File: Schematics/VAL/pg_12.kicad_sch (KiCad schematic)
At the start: 19 parts, among them U1401 F04, U1402 F04, U1403 F04, U1404 F04, U1405 F04, U1406 F04, U1407 F04, U1408 F04, U1409 F04, U1410 F04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

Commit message: Align to grid
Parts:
- removed U1401, U1402, U1403, U1404, U1405, U1406, U1407, U1408, U1409, U1410, U1411, U1412: F04, symbol r1000:F04
- removed U1413, U1414: F64, symbol r1000:F64
- removed U1415, U1416, U1417: F00, symbol r1000:F00
- removed U1418: F240, symbol r1000:F240
- removed U1419: F374, symbol r1000:F374
- added U (x12): (no value), symbol r1000:F04
- added U (x3): (no value), symbol r1000:F00
- added U: (no value), symbol r1000:F374
- added U (x2): (no value), symbol r1000:F64
- added U: (no value), symbol r1000:F240
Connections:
- net A.D48: now also U.18 (Y0)
- net A.D49: now also U.16 (Y1)
- net A.D50: now also U.14 (Y2)
- net A.D51: now also U.12 (Y3)
- net A.D52: now also U.9 (Y4)
- net A.D53: now also U.7 (Y5)
- net A.D54: now also U.5 (Y6)
- net A.D55: now also U.3 (Y7)
- net A.D56: now also U.2 (Q0)
- net A.D57: now also U.5 (Q1)
- net A.D58: now also U.6 (Q2)
- net A.D59: now also U.9 (Q3)
- net A.D60: now also U.12 (Q4)
- net A.D61: now also U.15 (Q5)
- net A.D62: now also U.16 (Q6)
- net A.D63: now also U.19 (Q7)
- net ALU.ZERO0: now also U.1 (D0)
- net ALU.ZERO1: now also U.1 (D0)
- net ALU.ZERO2: now also U.1 (D0)
- net ALU.ZERO3: now also U.1 (D0)
- net ALU.ZERO4: now also U.1 (D0)
- net ALU.ZERO5: now also U.1 (D0)
- net ALU.ZERO6: now also U.1 (D0)
- net ALU_32_Z~: now also U.1 (D0)
- net ALU_EQ_Z~: now also U.1 (D0), U.1 (D0), U.1 (D0), U.4 (D1)
- net PD: now also U.11 (I4), U.13 (I5), U.15 (I6), U.17 (I7), U.2 (I0), U.4 (I1), U.6 (I2), U.8 (I3)
- net PU: now also U.13 (D3), U.2 (A0), U.2 (A0), U.3 (D0), U.9 (B0)
- net ZERO.OE~: now also U.1 (OE), U.1 (OE0), U.19 (OE1)
- net ZERO_COUNT~1: now also U.3 (Q), U.7 (D2)
- net ZERO_COUNT~2: now also U.3 (Q), U.8 (D3)
- net ZERO_COUNT~3: now also U.13 (D4), U.3 (Q)
- net ZERO_COUNT~4: now also U.14 (D5)
- net ZERO_COUNT~5: now also U.17 (D6)
- net ZERO_COUNT~6: now also U.18 (D7)
- net ZERO~.SCLK: now also U.11 (CLK)
- net ZMUX.SEL0: now also U.2 (D1), U.2 (Q)
- net ZMUX.SEL1: now also U.2 (D1), U.8 (Q)
- net ZMUX.SEL2: now also U.2 (D1), U.8 (Q)
- new net: U.1 (D0), U.2 (Q), U.3 (A1)
- new net: U.10 (B1), U.13 (D3), U.2 (Q), U.6 (C2)
- new net: U.1 (D0), U.2 (Q), U.9 (B0)
- new net: U.1 (D0), U.2 (Q) (x2)
- new net: U.11 (D1), U.12 (D2), U.2 (Q), U.5 (C1), U.5 (C1)
- new net: U.11 (D1), U.2 (Q)
- new net: U.10 (B1), U.2 (Q), U.3 (A1)
- new net: U.1 (D0), U.2 (Q), U.4 (C0) (x2)
- new net: U.12 (D2), U.2 (Q), U.6 (C2)

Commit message: Tested to 6.81 seconds (rm071)
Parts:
- removed U (x12): (no value), symbol r1000:F04
- removed U (x3): (no value), symbol r1000:F00
- removed U: (no value), symbol r1000:F374
- removed U (x2): (no value), symbol r1000:F64
- removed U: (no value), symbol r1000:F240
- added U: (no value), symbol r1000:XZCNT
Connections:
- net A.D48: now also U.100 (Z48)
- net A.D49: now also U.102 (Z49)
- net A.D50: now also U.104 (Z50)
- net A.D51: now also U.106 (Z51)
- net A.D52: now also U.108 (Z52)
- net A.D53: now also U.110 (Z53)
- net A.D54: now also U.112 (Z54)
- net A.D55: now also U.114 (Z55)
- net A.D56: now also U.116 (Z56)
- net A.D57: now also U.118 (Z57)
- net A.D58: now also U.120 (Z58)
- net A.D59: now also U.122 (Z59)
- net A.D60: now also U.124 (Z60)
- net A.D61: now also U.126 (Z61)
- net A.D62: now also U.128 (Z62)
- net A.D63: now also U.130 (Z63)
- net ZERO.OE~: now also U.2 (OE)
- net ZERO~.SCLK: now also U.1 (CLK)
- new net A.D0: U.4 (Z0)
- new net A.D1: U.6 (Z1)
- new net A.D10: U.24 (Z10)
- new net A.D11: U.26 (Z11)
- new net A.D12: U.28 (Z12)
- new net A.D13: U.30 (Z13)
- new net A.D14: U.32 (Z14)
- new net A.D15: U.34 (Z15)
- new net A.D16: U.36 (Z16)
- new net A.D17: U.38 (Z17)
- new net A.D18: U.40 (Z18)
- new net A.D19: U.42 (Z19)
- new net A.D2: U.8 (Z2)
- new net A.D20: U.44 (Z20)
- new net A.D21: U.46 (Z21)
- new net A.D22: U.48 (Z22)
- new net A.D23: U.50 (Z23)
- new net A.D24: U.52 (Z24)
- new net A.D25: U.54 (Z25)
- new net A.D26: U.56 (Z26)
- new net A.D27: U.58 (Z27)
- new net A.D28: U.60 (Z28)
- new net A.D29: U.62 (Z29)
- new net A.D3: U.10 (Z3)
- new net A.D30: U.64 (Z30)
- new net A.D31: U.66 (Z31)
- new net A.D32: U.68 (Z32)
- new net A.D33: U.70 (Z33)
- new net A.D34: U.72 (Z34)
- new net A.D35: U.74 (Z35)
- new net A.D36: U.76 (Z36)
- new net A.D37: U.78 (Z37)
- new net A.D38: U.80 (Z38)
- new net A.D39: U.82 (Z39)
- new net A.D4: U.12 (Z4)
- new net A.D40: U.84 (Z40)
- new net A.D41: U.86 (Z41)
- new net A.D42: U.88 (Z42)
- new net A.D43: U.90 (Z43)
- new net A.D44: U.92 (Z44)
- new net A.D45: U.94 (Z45)
- new net A.D46: U.96 (Z46)
- new net A.D47: U.98 (Z47)
- new net A.D5: U.14 (Z5)
- new net A.D6: U.16 (Z6)
- new net A.D7: U.18 (Z7)
- new net A.D8: U.20 (Z8)
- new net A.D9: U.22 (Z9)
- new net ALU.D0: U.3 (I0)
- new net ALU.D1: U.5 (I1)
- new net ALU.D10: U.23 (I10)
- new net ALU.D11: U.25 (I11)
- new net ALU.D12: U.27 (I12)
- new net ALU.D13: U.29 (I13)
- new net ALU.D14: U.31 (I14)
- new net ALU.D15: U.33 (I15)
- new net ALU.D16: U.35 (I16)
- new net ALU.D17: U.37 (I17)
- new net ALU.D18: U.39 (I18)
- new net ALU.D19: U.41 (I19)
- new net ALU.D2: U.7 (I2)
- new net ALU.D20: U.43 (I20)
- new net ALU.D21: U.45 (I21)
- new net ALU.D22: U.47 (I22)
- new net ALU.D23: U.49 (I23)
- new net ALU.D24: U.51 (I24)
- new net ALU.D25: U.53 (I25)
- new net ALU.D26: U.55 (I26)
- new net ALU.D27: U.57 (I27)
- new net ALU.D28: U.59 (I28)
- new net ALU.D29: U.61 (I29)
- new net ALU.D3: U.9 (I3)
- new net ALU.D30: U.63 (I30)
- new net ALU.D31: U.65 (I31)
- new net ALU.D32: U.67 (I32)
- new net ALU.D33: U.69 (I33)
- new net ALU.D34: U.71 (I34)
- new net ALU.D35: U.73 (I35)
- new net ALU.D36: U.75 (I36)
- new net ALU.D37: U.77 (I37)
- new net ALU.D38: U.79 (I38)
- new net ALU.D39: U.81 (I39)
- new net ALU.D4: U.11 (I4)
- new net ALU.D40: U.83 (I40)
- new net ALU.D41: U.85 (I41)
- new net ALU.D42: U.87 (I42)
- new net ALU.D43: U.89 (I43)
- new net ALU.D44: U.91 (I44)
- new net ALU.D45: U.93 (I45)
- new net ALU.D46: U.95 (I46)
- new net ALU.D47: U.97 (I47)
- new net ALU.D48: U.99 (I48)
- new net ALU.D49: U.101 (I49)
- new net ALU.D5: U.13 (I5)
- new net ALU.D50: U.103 (I50)
- new net ALU.D51: U.105 (I51)
- new net ALU.D52: U.107 (I52)
- new net ALU.D53: U.109 (I53)
- new net ALU.D54: U.111 (I54)
- new net ALU.D55: U.113 (I55)
- new net ALU.D56: U.115 (I56)
- new net ALU.D57: U.117 (I57)
- new net ALU.D58: U.119 (I58)
- new net ALU.D59: U.121 (I59)
- new net ALU.D6: U.15 (I6)
- new net ALU.D60: U.123 (I60)
- new net ALU.D61: U.125 (I61)
- new net ALU.D62: U.127 (I62)
- new net ALU.D63: U.129 (I63)
- new net ALU.D7: U.17 (I7)
- new net ALU.D8: U.19 (I8)
- new net ALU.D9: U.21 (I9)

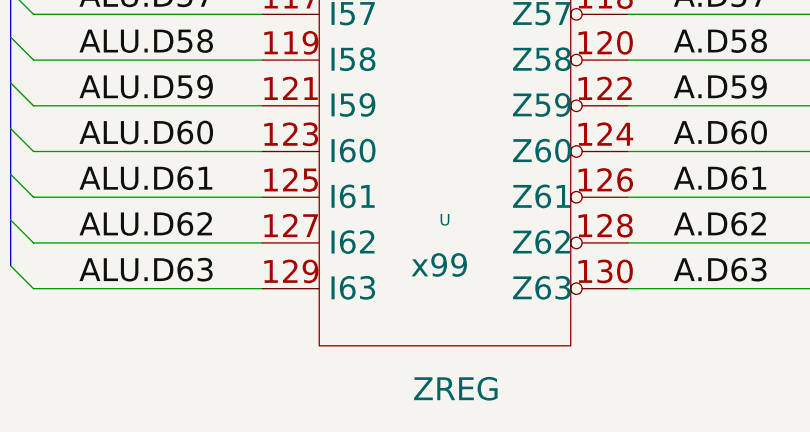
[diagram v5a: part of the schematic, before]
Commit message: Eliminate empty pages
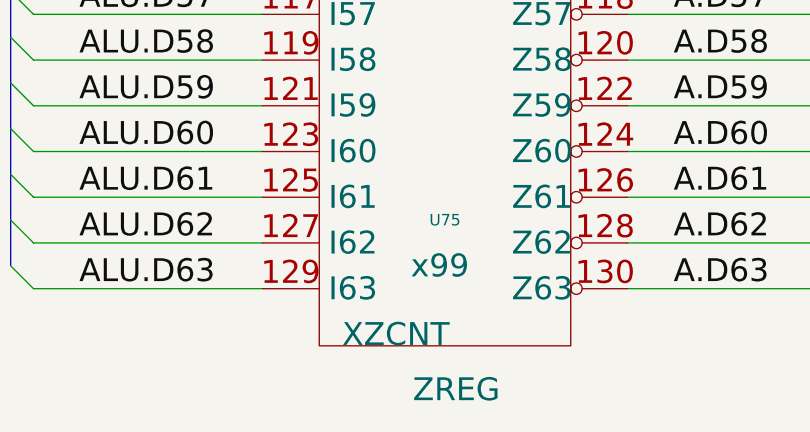
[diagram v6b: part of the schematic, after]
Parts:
- U75: renamed from U; value (none) -> XZCNT
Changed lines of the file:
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@@
-(kicad_sch (version 20220404) (generator eeschema)
+(kicad_sch (version 20221206) (generator eeschema)
   (paper "User" 584.2 378.46)
   (title_block
@@
   (global_label "ALU.D[0..63]" (shape input) (at 228.6 33.02 180) (fields_autoplaced)
     (effects (font (size 2.54 2.54)) (justify right))
-    (property "Intersheet References" "${INTERSHEET_REFS}" (id 0) (at 200.0673 32.8613 0)
+    (property "Intersheetrefs" "${INTERSHEET_REFS}" (at 200.0673 32.8613 0)
       (effects (font (size 1.905 1.905)) (justify right))
     )
@@
   (global_label "ZERO.OE~" (shape input) (at 307.34 27.94 0) (fields_autoplaced)
     (effects (font (size 2.54 2.54)) (justify left))
-    (property "Intersheet References" "${INTERSHEET_REFS}" (id 0) (at 330.067 27.7813 0)
+    (property "Intersheetrefs" "${INTERSHEET_REFS}" (at 330.067 27.7813 0)
       (effects (font (size 1.905 1.905)) (justify left))
     )
@@
   (global_label "A.D[0..63]" (shape output) (at 332.74 33.02 0) (fields_autoplaced)
     (effects (font (size 2.54 2.54)) (justify left))
-    (property "Intersheet References" "${INTERSHEET_REFS}" (id 0) (at 356.5555 32.8613 0)
+    (property "Intersheetrefs" "${INTERSHEET_REFS}" (at 356.5555 32.8613 0)
       (effects (font (size 1.905 1.905)) (justify left))
     )
@@
   (global_label "ZERO~.SCLK" (shape input) (at 256.54 27.94 180) (fields_autoplaced)
     (effects (font (size 2.54 2.54)) (justify right))
-    (property "Intersheet References" "${INTERSHEET_REFS}" (id 0) (at 229.2169 27.7813 0)
+    (property "Intersheetrefs" "${INTERSHEET_REFS}" (at 229.2169 27.7813 0)
       (effects (font (size 1.905 1.905)) (justify right))
     )
   )
   (symbol (lib_id "r1000:XZCNT") (at 279.4 353.06 0) (unit 1)
-    (in_bom yes) (on_board yes)
-    (default_instance (reference "U") (unit 1) (value "") (footprint ""))
-    (property "Reference" "U" (id 0) (at 281.94 347.98 0)
+    (in_bom yes) (on_board yes) (dnp no)
+    (property "Reference" "U75" (at 281.94 347.98 0)
       (effects (font (size 1.27 1.27)))
     )
-    (property "Value" "" (id 1) (at 270.51 360.68 0)
+    (property "Value" "XZCNT" (at 270.51 360.68 0)
       (effects (font (size 2.54 2.54)) (justify left))
     )
-    (property "Footprint" "" (id 2) (at 280.67 354.33 0)
+    (property "Footprint" "" (at 280.67 354.33 0)
       (effects (font (size 1.27 1.27)) hide)
     )
-    (property "Datasheet" "" (id 3) (at 280.67 354.33 0)
+    (property "Datasheet" "" (at 280.67 354.33 0)
       (effects (font (size 1.27 1.27)) hide)
     )
-    (property "Location" "x99" (id 4) (at 278.13 353.06 0)
+    (property "Location" "x99" (at 278.13 353.06 0)
       (effects (font (size 2.54 2.54)) (justify left))
     )
-    (property "Name" "ZREG" (id 5) (at 283.21 368.3 0)
+    (property "Name" "ZREG" (at 283.21 368.3 0)
       (effects (font (size 2.54 2.54)) (justify bottom))
     )
@@
     (pin "98")
     (pin "99")
+    (instances
+      (project "VAL"
+        (path "/20011966-0b12-5e7d-4f5d-7b7451992361/20011966-2970-3247-598a-45c7a18973dc"
+          (reference "U75") (unit 1)
+        )
+      )
+    )
   )
 )
